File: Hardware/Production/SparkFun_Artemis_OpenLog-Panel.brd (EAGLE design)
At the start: 137.2 x 167 mm, 1942 parts, among them J105 CORTEX_JTAG, J106 MICRO-SD, J113 CORTEX_JTAG, J114 MICRO-SD, J121 CORTEX_JTAG, J122 MICRO-SD, J14 CORTEX_JTAG, J16 CORTEX_JTAG, J17 MICRO-SD, J18 MICRO-SD, J25 CORTEX_JTAG, J26 MICRO-SD, J33 CORTEX_JTAG, J34 MICRO-SD, J41 CORTEX_JTAG, J42 MICRO-SD, J49 CORTEX_JTAG, J50 MICRO-SD, J57 CORTEX_JTAG, J58 MICRO-SD, J6 CORTEX_JTAG, J65 CORTEX_JTAG, J66 MICRO-SD, J7 MICRO-SD, J73 CORTEX_JTAG, J74 MICRO-SD, J81 CORTEX_JTAG, J82 MICRO-SD, J89 CORTEX_JTAG, J90 MICRO-SD, J97 CORTEX_JTAG, J98 MICRO-SD, Q1 20V/0.2A/8MHz/1.2Ω/1Vth, Q10 20V/0.2A/8MHz/1.2Ω/1Vth, Q100 20V/0.2A/8MHz/1.2Ω/1Vth, Q101 20V/0.2A/8MHz/1.2Ω/1Vth, Q102 20V/0.2A/8MHz/1.2Ω/1Vth, Q103 20V/0.2A/8MHz/1.2Ω/1Vth, Q104 20V/4.2A/52mΩ/1.4W, Q105 20V/4.2A/52mΩ/1.4W, Q106 20V/0.2A/8MHz/1.2Ω/1Vth, Q107 20V/0.2A/8MHz/1.2Ω/1Vth, Q108 20V/0.2A/8MHz/1.2Ω/1Vth, Q109 20V/0.2A/8MHz/1.2Ω/1Vth, Q11 20V/0.2A/8MHz/1.2Ω/1Vth, Q110 20V/0.2A/8MHz/1.2Ω/1Vth, Q111 20V/4.2A/52mΩ/1.4W, Q112 20V/4.2A/52mΩ/1.4W, Q12 20V/0.2A/8MHz/1.2Ω/1Vth, Q13 20V/4.2A/52mΩ/1.4W, Q14 20V/4.2A/52mΩ/1.4W, Q15 20V/0.2A/8MHz/1.2Ω/1Vth, Q16 20V/0.2A/8MHz/1.2Ω/1Vth, Q17 20V/0.2A/8MHz/1.2Ω/1Vth, Q18 20V/0.2A/8MHz/1.2Ω/1Vth, Q19 20V/0.2A/8MHz/1.2Ω/1Vth, Q2 20V/4.2A/52mΩ/1.4W, Q20 20V/4.2A/52mΩ/1.4W, Q21 20V/4.2A/52mΩ/1.4W, Q22 20V/0.2A/8MHz/1.2Ω/1Vth, Q23 20V/0.2A/8MHz/1.2Ω/1Vth, Q24 20V/0.2A/8MHz/1.2Ω/1Vth, Q25 20V/0.2A/8MHz/1.2Ω/1Vth, Q26 20V/0.2A/8MHz/1.2Ω/1Vth, Q27 20V/4.2A/52mΩ/1.4W, Q28 20V/4.2A/52mΩ/1.4W, Q29 20V/0.2A/8MHz/1.2Ω/1Vth, Q3 20V/0.2A/8MHz/1.2Ω/1Vth, Q30 20V/0.2A/8MHz/1.2Ω/1Vth, Q31 20V/0.2A/8MHz/1.2Ω/1Vth, Q32 20V/0.2A/8MHz/1.2Ω/1Vth, Q33 20V/0.2A/8MHz/1.2Ω/1Vth, Q34 20V/4.2A/52mΩ/1.4W, Q35 20V/4.2A/52mΩ/1.4W, Q36 20V/0.2A/8MHz/1.2Ω/1Vth, Q37 20V/0.2A/8MHz/1.2Ω/1Vth, Q38 20V/0.2A/8MHz/1.2Ω/1Vth, Q39 20V/0.2A/8MHz/1.2Ω/1Vth, Q4 20V/4.2A/52mΩ/1.4W, Q40 20V/0.2A/8MHz/1.2Ω/1Vth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

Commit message: Added production files
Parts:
- removed JP17, JP19, JP21, JP23, JP25, JP27, JP29, JP31: (no value), SparkFun-Jumpers:SMT-JUMPER_2_NC_TRACE_SILK
- removed JP18, JP20, JP22, JP24, JP26, JP28, JP30, JP32: MEAS, SparkFun-Jumpers:COMBO-JUMPER_2_NC_TRACE
- removed Q100, Q101, Q102, Q103, Q106, Q107, Q108, Q109, Q110, Q99: 20V/0.2A/8MHz/1.2Ω/1Vth, SparkFun-DiscreteSemi:SOT-416FL
- removed Q104, Q105, Q111, Q112, Q97, Q98: 20V/4.2A/52mΩ/1.4W, SparkFun-DiscreteSemi:SOT23-3
- added J129, J138: (no value), SparkFun-Connectors:JST-2-SMD
- added J130, J133, J139, J142: (no value), SparkFun-Connectors:1X02_NO_SILK
- added J131, J140: (no value), SparkFun-Connectors:1X06_NO_SILK
- added J132, J141: (no value), USBC:USB-C-16P-5
- added J134, J143: MICRO-SD, SparkFun-Connectors:MICRO-SD-SOCKET
- added J135, J144: (no value), SparkFun-Connectors:1X01_NO_SILK
- added J136: CORTEX_JTAG, SparkFun-Connectors:2X5-PTH-1.27MM
- added J137: (no value), SparkFun-Connectors:JST04_1MM_RA
- added LOGO17, LOGO21, LOGO25, LOGO29, LOGO33, LOGO37, LOGO41, LOGO45, LOGO49, LOGO53, LOGO57, LOGO61: OSHW-LOGOS, SparkFun-Aesthetics:OSHW-LOGO-S
- added LOGO18, LOGO20, LOGO22, LOGO24, LOGO26, LOGO28, LOGO30, LOGO32, LOGO34, LOGO36, LOGO38, LOGO40, LOGO42, LOGO44, LOGO46, LOGO48, LOGO50, LOGO52, LOGO54, LOGO56, LOGO58, LOGO60, LOGO62, LOGO64: SFE_LOGO_FLAME.1_INCH, SparkFun-Aesthetics:SFE_LOGO_FLAME_.1
- added LOGO19, LOGO23, LOGO27, LOGO31, LOGO35, LOGO39, LOGO43, LOGO47, LOGO51, LOGO55, LOGO59, LOGO63: SFE_LOGO_NAME.1_INCH, SparkFun-Aesthetics:SFE_LOGO_NAME_.1
- added R321, R344, R367: 1M, New_Parts:0402-TIGHT
- added R322, R345, R368: 2M, New_Parts:0402-TIGHT
- added R323, R333, R334, R335, R336, R337, R338, R339, R346, R356, R357, R358, R359, R360, R361, R362: 2.2k, SparkFun-Resistors:0402-TIGHT
- added R324, R325, R326, R327, R328, R341, R347, R348, R349, R350, R351, R364: 1k, SparkFun-Resistors:0402-TIGHT
- added R329, R330, R352, R353: 5.1k, SparkFun-Resistors:0402-TIGHT
- added R331, R354: 100k, SparkFun-Resistors:0402-TIGHT
- added R332, R355: 220KOHM-0402T-1/16W-1%, SparkFun-Resistors:0402-TIGHT
- added R340, R363: DNP, SparkFun-Resistors:0402-TIGHT
- added R342, R365: 330K, New_Parts:0402-TIGHT
- added R343, R366: 220k, SparkFun-Resistors:0402-TIGHT
- added U$577: (no value), buzzard_labels (14):3V34
- added U$578, U$579: (no value), buzzard_labels (14):113
- added U$580, U$581: (no value), buzzard_labels (14):322
- added U$582, U$583: (no value), buzzard_labels (14):GND5
- added U$584, U$585: (no value), buzzard_labels (14):RX1
- added U$586, U$587: (no value), buzzard_labels (14):TX0
- added U$588, U$589: (no value), buzzard_labels:PSWC0
- added U$590: (no value), buzzard_labels (19):VE0
- added U$591, U$592: (no value), RST_04:RST0
- added U113, U121: MCP73831, SparkFun-IC-Power:SOT23-5
- added U114, U122: ARTEMIS_MODULE, SparkFun-IC-Microcontroller:ARTEMIS_FP
- added U115, U123: CH340E, SparkFun-IC-Comms:MSOP10
- added U116, U124: ICM-20948, SparkFun-Sensors:QFN24-3X3
- added U117, U125: 1.8V/100mA, SparkFun-IC-Power:SC70
- added U118, U120, U126, U128: AP2112K, SparkFun-IC-Power:SOT23-5
- added U119, U127: 3.0V Supervisor, SparkFun-IC-Power:SOT23-3
- added VE, VE1, VE10, VE11, VE12, VE13, VE14, VE15, VE2, VE3, VE4, VE5, VE6, VE7, VE8, VE9: (no value), SparkFun-Jumpers:SMT-JUMPER_2_NO_SILK
- C1, C102, C103, C111, C113, C12, C123, C124, C132, C134, C14, C144, C145, C153, C155, C165, C166, C174, C176, C186, C187, C195, C197, C2, C207, C208, C216, C218, C228, C229, C237, C239, C24, C249, C25, C250, C258, C260, C270, C271, C279, C281, C291, C292, C300, C302, C312, C313, C32, C321, C323, C333, C334, C38, C40, C45, C60, C61, C69, C71, C81, C82, C90, C92: device SparkFun-Capacitors:0603 -> SparkFun-Capacitors:0402-TIGHT
- C104, C125, C146, C167, C188, C209, C230, C251, C26, C272, C293, C314, C335, C5, C62, C83: value 10uF -> 0.1uF; device SparkFun-Capacitors:0603 -> SparkFun-Capacitors:0402-TIGHT
- C105, C126, C147, C168, C189, C210, C231, C252, C27, C273, C294, C315, C336, C63, C84: value 1.0uF -> 2.2uF
- C6: value 1.0uF -> 4.7uF
- C7: value 4.7uF -> 2.2uF
- J10, J120, J21, J48, J93: device SparkFun-Connectors:1X02_NO_SILK -> SparkFun-Connectors:JST-2-SMD
- J100, J28: value (none) -> CORTEX_JTAG; device SparkFun-Connectors:JST-2-SMD -> SparkFun-Connectors:2X5-PTH-1.27MM
- J101, J128, J29, J56: device SparkFun-Connectors:1X02_NO_SILK -> SparkFun-Connectors:JST04_1MM_RA
- J102, J30: device SparkFun-Connectors:1X06_NO_SILK -> SparkFun-Connectors:JST-2-SMD
- J103, J31, J79: device USBC:USB-C-16P-5 -> SparkFun-Connectors:1X02_NO_SILK
- J104, J32, J77: device SparkFun-Connectors:1X02_NO_SILK -> SparkFun-Connectors:1X06_NO_SILK
- J105, J33: value CORTEX_JTAG -> (none); device SparkFun-Connectors:2X5-PTH-1.27MM -> USBC:USB-C-16P-5
- J106, J34, J58: value MICRO-SD -> (none); device SparkFun-Connectors:MICRO-SD-SOCKET -> SparkFun-Connectors:1X02_NO_SILK
- J107, J35: value (none) -> MICRO-SD; device SparkFun-Connectors:JST04_1MM_RA -> SparkFun-Connectors:MICRO-SD-SOCKET
- J108, J36: device SparkFun-Connectors:JST-2-SMD -> SparkFun-Connectors:1X01_NO_SILK
- J109, J37, J64: value (none) -> CORTEX_JTAG; device SparkFun-Connectors:1X02_NO_SILK -> SparkFun-Connectors:2X5-PTH-1.27MM
- J110, J38: device SparkFun-Connectors:1X06_NO_SILK -> SparkFun-Connectors:JST04_1MM_RA
- J111, J39: device USBC:USB-C-16P-5 -> SparkFun-Connectors:JST-2-SMD
- J113, J41: value CORTEX_JTAG -> (none); device SparkFun-Connectors:2X5-PTH-1.27MM -> SparkFun-Connectors:1X06_NO_SILK
- J114, J42: value MICRO-SD -> (none); device SparkFun-Connectors:MICRO-SD-SOCKET -> USBC:USB-C-16P-5
- J115, J43, J67: device SparkFun-Connectors:JST04_1MM_RA -> SparkFun-Connectors:1X02_NO_SILK
- J116, J44: value (none) -> MICRO-SD; device SparkFun-Connectors:JST-2-SMD -> SparkFun-Connectors:MICRO-SD-SOCKET
- J117, J45, J72: device SparkFun-Connectors:1X02_NO_SILK -> SparkFun-Connectors:1X01_NO_SILK
- J118, J46: value (none) -> CORTEX_JTAG; device SparkFun-Connectors:1X06_NO_SILK -> SparkFun-Connectors:2X5-PTH-1.27MM
- J119, J47: device USBC:USB-C-16P-5 -> SparkFun-Connectors:JST04_1MM_RA
- J12, J22, J70, J94: device SparkFun-Connectors:1X06_NO_SILK -> SparkFun-Connectors:1X02_NO_SILK
- J121, J16, J25, J49, J97: value CORTEX_JTAG -> (none); device SparkFun-Connectors:2X5-PTH-1.27MM -> SparkFun-Connectors:1X02_NO_SILK
- J122, J50: value MICRO-SD -> (none); device SparkFun-Connectors:MICRO-SD-SOCKET -> SparkFun-Connectors:1X06_NO_SILK
- J123, J51: device SparkFun-Connectors:JST04_1MM_RA -> USBC:USB-C-16P-5
- J124, J52, J76: device SparkFun-Connectors:JST-2-SMD -> SparkFun-Connectors:1X02_NO_SILK
- J125, J53, J80: value (none) -> MICRO-SD; device SparkFun-Connectors:1X02_NO_SILK -> SparkFun-Connectors:MICRO-SD-SOCKET
- J126, J54: device SparkFun-Connectors:1X06_NO_SILK -> SparkFun-Connectors:1X01_NO_SILK
- J127, J55: value (none) -> CORTEX_JTAG; device USBC:USB-C-16P-5 -> SparkFun-Connectors:2X5-PTH-1.27MM
- J13, J23, J95: device USBC:USB-C-16P-5 -> SparkFun-Connectors:1X06_NO_SILK
- J15, J24, J69, J96: device SparkFun-Connectors:1X02_NO_SILK -> USBC:USB-C-16P-5
- J18, J7, J90: value MICRO-SD -> (none); device SparkFun-Connectors:MICRO-SD-SOCKET -> SparkFun-Connectors:1X01_NO_SILK
- J19, J8, J91: value (none) -> CORTEX_JTAG; device SparkFun-Connectors:JST04_1MM_RA -> SparkFun-Connectors:2X5-PTH-1.27MM
- J20, J9, J92: device SparkFun-Connectors:JST-2-SMD -> SparkFun-Connectors:JST04_1MM_RA
- J27, J99: device SparkFun-Connectors:JST04_1MM_RA -> SparkFun-Connectors:1X01_NO_SILK
- J57: value CORTEX_JTAG -> (none); device SparkFun-Connectors:2X5-PTH-1.27MM -> SparkFun-Connectors:JST-2-SMD
- J59: device SparkFun-Connectors:JST04_1MM_RA -> SparkFun-Connectors:1X06_NO_SILK
- J6, J89: value CORTEX_JTAG -> MICRO-SD; device SparkFun-Connectors:2X5-PTH-1.27MM -> SparkFun-Connectors:MICRO-SD-SOCKET
- J60: device SparkFun-Connectors:JST-2-SMD -> USBC:USB-C-16P-5
- J62: value (none) -> MICRO-SD; device SparkFun-Connectors:1X06_NO_SILK -> SparkFun-Connectors:MICRO-SD-SOCKET
- J63: device USBC:USB-C-16P-5 -> SparkFun-Connectors:1X01_NO_SILK
- J65: value CORTEX_JTAG -> (none); device SparkFun-Connectors:2X5-PTH-1.27MM -> SparkFun-Connectors:JST04_1MM_RA
- J66: value MICRO-SD -> (none); device SparkFun-Connectors:MICRO-SD-SOCKET -> SparkFun-Connectors:JST-2-SMD
- J68: device SparkFun-Connectors:JST-2-SMD -> SparkFun-Connectors:1X06_NO_SILK
- J71: value (none) -> MICRO-SD; device USBC:USB-C-16P-5 -> SparkFun-Connectors:MICRO-SD-SOCKET
- J74: value MICRO-SD -> (none); device SparkFun-Connectors:MICRO-SD-SOCKET -> SparkFun-Connectors:JST04_1MM_RA
- J75: device SparkFun-Connectors:JST04_1MM_RA -> SparkFun-Connectors:JST-2-SMD
- J78: device SparkFun-Connectors:1X06_NO_SILK -> USBC:USB-C-16P-5
- J81: value CORTEX_JTAG -> (none); device SparkFun-Connectors:2X5-PTH-1.27MM -> SparkFun-Connectors:1X01_NO_SILK
- J82: value MICRO-SD -> CORTEX_JTAG; device SparkFun-Connectors:MICRO-SD-SOCKET -> SparkFun-Connectors:2X5-PTH-1.27MM
- JP1, JP11, JP13, JP15, JP3, JP5, JP7, JP9: value (none) -> MEAS; device SparkFun-Jumpers:SMT-JUMPER_2_NC_TRACE_SILK -> SparkFun-Jumpers:COMBO-JUMPER_2_NC_TRACE
- LOGO1, LOGO11, LOGO15, LOGO7: value OSHW-LOGOS -> SFE_LOGO_NAME.1_INCH; device SparkFun-Aesthetics:OSHW-LOGO-S -> SparkFun-Aesthetics:SFE_LOGO_NAME_.1
- LOGO10, LOGO12, LOGO14, LOGO16, LOGO4, LOGO5, LOGO6, LOGO8: value OSHW-LOGOS -> SFE_LOGO_FLAME.1_INCH; device SparkFun-Aesthetics:OSHW-LOGO-S -> SparkFun-Aesthetics:SFE_LOGO_FLAME_.1
- Q12, Q18, Q24, Q30, Q36, Q54, Q60, Q66, Q72, Q78, Q96: value 20V/0.2A/8MHz/1.2Ω/1Vth -> 20V/4.2A/52mΩ/1.4W; device SparkFun-DiscreteSemi:SOT-416FL -> SparkFun-DiscreteSemi:SOT23-3
- Q13, Q14, Q20, Q21, Q27, Q28, Q34, Q35, Q4, Q41, Q49, Q55, Q56, Q62, Q63, Q69, Q70, Q76, Q77, Q83, Q91: value 20V/4.2A/52mΩ/1.4W -> 20V/0.2A/8MHz/1.2Ω/1Vth; device SparkFun-DiscreteSemi:SOT23-3 -> SparkFun-DiscreteSemi:SOT-416FL
- R100, R260: value 10k -> 5.1k
- R101, R16, R193, R216, R55, R78: value 2.2k -> 100k
- R102, R125, R263, R286, R79: value 1k -> 220KOHM-0402T-1/16W-1%
- R103, R104, R105, R106, R126, R139, R162, R185, R199, R219, R222, R223, R224, R242, R243, R244, R245, R246, R264, R265, R266, R31, R59, R62, R63, R8, R82, R83, R84, R85, R86: value 1k -> 2.2k
- R107, R108, R127, R128, R208, R247, R267, R268, R287, R288, R39: value 5.1k -> 2.2k
- R109, R129, R149, R269, R289: value 100k -> 2.2k
- R11, R12, R167, R187, R188, R42, R88: value 5.1k -> 1k
- R110: value 220k -> DNP; device SparkFun-Resistors:0603 -> SparkFun-Resistors:0402-TIGHT
- R111, R117, R118, R121, R134, R141, R157, R211, R212, R213, R232, R233, R234, R235, R236, R255, R256, R257, R258, R272, R278, R281, R295, R301, R318, R51, R52, R71, R72, R73, R74, R75, R94, R95, R96, R97, R98: value 2.2k -> 1k
- R112, R135, R158, R181, R273, R296: value 2.2k -> 330K; device SparkFun-Resistors:0402-TIGHT -> New_Parts:0402-TIGHT
- R113, R136, R251, R274, R297, R3: value 2.2k -> 220k
- R114, R137, R252, R275, R298, R91: value 2.2k -> 1M; device SparkFun-Resistors:0402-TIGHT -> New_Parts:0402-TIGHT
- R115, R138, R161, R253, R276, R92: value 2.2k -> 2M; device SparkFun-Resistors:0402-TIGHT -> New_Parts:0402-TIGHT
- R120, R140, R180, R280: value 10k -> 1k
- R122, R123, R145, R146, R283, R284, R306, R99: value 1k -> 5.1k
- R124, R239, R262, R285: value 1k -> 100k
- R13, R189, R209, R249, R43: value 100k -> 1k
- R130, R150, R270, R290, R310, R70: value 220k -> 2.2k; device SparkFun-Resistors:0603 -> SparkFun-Resistors:0402-TIGHT
- R133, R156, R271, R294, R317, R33, R49: value 2.2k -> DNP
- R14: value 220k -> 5.1k; device SparkFun-Resistors:0603 -> SparkFun-Resistors:0402-TIGHT
- R147, R308: value 5.1k -> 100k
- R148: value 5.1k -> 220KOHM-0402T-1/16W-1%
- R15, R191, R192, R214, R215, R237, R238, R261, R53, R54, R76, R77: value 2.2k -> 5.1k
- R159, R182, R205, R36: value 1k -> 220k
- R160: value 10k -> 1M; device SparkFun-Resistors:0402-TIGHT -> New_Parts:0402-TIGHT
- R169: value 100k -> 5.1k
- R17, R171, R194, R217, R56: value 2.2k -> 220KOHM-0402T-1/16W-1%
- R170: value 220k -> 100k; device SparkFun-Resistors:0603 -> SparkFun-Resistors:0402-TIGHT
- R179, R202, R225, R64: value 1k -> DNP
- R183, R206, R37, R6: value 1k -> 1M; device SparkFun-Resistors:0402-TIGHT -> New_Parts:0402-TIGHT
- R184, R299, R38, R7: value 1k -> 2M; device SparkFun-Resistors:0402-TIGHT -> New_Parts:0402-TIGHT
- R190, R210, R50: value 220k -> 1k; device SparkFun-Resistors:0603 -> SparkFun-Resistors:0402-TIGHT
- R2: value 10k -> 330K; device SparkFun-Resistors:0402-TIGHT -> New_Parts:0402-TIGHT
- R200, R220, R300, R32, R60, R80: value 10k -> 2.2k
- R204, R319, R35, R66: value 1k -> 330K; device SparkFun-Resistors:0402-TIGHT -> New_Parts:0402-TIGHT
- R207: value 5.1k -> 2M; device SparkFun-Resistors:0402-TIGHT -> New_Parts:0402-TIGHT
- R227: value 5.1k -> 330K; device SparkFun-Resistors:0402-TIGHT -> New_Parts:0402-TIGHT
- R228, R67: value 5.1k -> 220k
- R229: value 100k -> 1M; device SparkFun-Resistors:0402-TIGHT -> New_Parts:0402-TIGHT
- R230: value 220k -> 2M; device SparkFun-Resistors:0603 -> New_Parts:0402-TIGHT
- R240: value 10k -> 220KOHM-0402T-1/16W-1%
- R248, R87: value 5.1k -> DNP
- R250: value 220k -> 330K; device SparkFun-Resistors:0603 -> New_Parts:0402-TIGHT
- R29: value 220k -> 220KOHM-0402T-1/16W-1%; device SparkFun-Resistors:0603 -> SparkFun-Resistors:0402-TIGHT
- R309: value 100k -> 220KOHM-0402T-1/16W-1%
- R320: value 10k -> 220k
- R68: value 5.1k -> 1M; device SparkFun-Resistors:0402-TIGHT -> New_Parts:0402-TIGHT
- R69: value 100k -> 2M; device SparkFun-Resistors:0402-TIGHT -> New_Parts:0402-TIGHT
- R89: value 100k -> 330K; device SparkFun-Resistors:0402-TIGHT -> New_Parts:0402-TIGHT
- R90: device SparkFun-Resistors:0603 -> SparkFun-Resistors:0402-TIGHT
- U$100, U$136, U$63, U$99: device buzzard_labels (14):GND5 -> buzzard_labels (14):322
- U$101, U$102, U$138, U$65: device buzzard_labels (14):RX1 -> buzzard_labels (14):GND5
- U$103, U$104, U$140, U$67: device buzzard_labels (14):TX0 -> buzzard_labels (14):RX1
- U$105, U$69: value SPARKX-LOGO3 -> (none); device SparkX:SPARKX-SMALL -> buzzard_labels (14):TX0
- U$106, U$142: device buzzard_labels (15):LED0 -> buzzard_labels (14):TX0
- U$109: device buzzard_labels (2):MEAS3 -> buzzard_labels (19):VE0
- U$110, U$296, U$332, U$74: device buzzard_labels (1):X0 -> RST_04:RST0
- U$111, U$147, U$333, U$369: device buzzard_labels (1):Y1 -> RST_04:RST0
- U$112, U$334: device buzzard_labels (1):Z2 -> buzzard_labels (2):MEAS3
- U$113: device buzzard_labels (1):G5 -> buzzard_labels (1):X0
- U$114: device buzzard_labels (1):A4 -> buzzard_labels (1):Y1
- U$115: device buzzard_labels (1):M3 -> buzzard_labels (1):Z2
- U$116: device buzzard_labels (1):X0 -> buzzard_labels (1):G5
- U$117: device buzzard_labels (1):Y1 -> buzzard_labels (1):A4
- U$118: device buzzard_labels (1):Z2 -> buzzard_labels (1):M3
- U$119, U$335: device qwiic#logo#jpg:QWIIC#LOGO#JPG -> buzzard_labels (1):X0
- U$12, U$73: device buzzard_labels (2):MEAS3 -> RST_04:RST0
- U$120, U$336: device buzzard_labels (12):CHG2 -> buzzard_labels (1):Y1
- U$121, U$337: device buzzard_labels (12):PWR0 -> buzzard_labels (1):Z2
- U$122: device buzzard_labels (12):RX4 -> qwiic#logo#jpg:QWIIC#LOGO#JPG
- U$123: device buzzard_labels (12):STAT5 -> buzzard_labels (12):CHG2
- U$124: device buzzard_labels (12):TX3 -> buzzard_labels (12):PWR0
- U$125: device buzzard_labels (13):ARTEMIS13 -> buzzard_labels (12):RX4
- U$126: device buzzard_labels (13):OPENLOG12 -> buzzard_labels (12):STAT5
- U$127: device buzzard_labels (13):RST9 -> buzzard_labels (12):TX3
- U$128: device buzzard_labels (13):VIN8 -> buzzard_labels (13):ARTEMIS13
- U$129, U$166: device buzzard_labels (14):3V34 -> buzzard_labels (13):OPENLOG12
- U$13, U$260: device buzzard_labels (1):X0 -> buzzard_labels (2):MEAS3
- U$130, U$93: device buzzard_labels (14):3V34 -> buzzard_labels (13):RST9
- U$131, U$168: device buzzard_labels (14):113 -> buzzard_labels (13):VIN8
- U$132, U$59, U$95, U$96: device buzzard_labels (14):113 -> buzzard_labels (14):3V34
- U$133, U$169, U$170, U$206: device buzzard_labels (14):322 -> buzzard_labels (14):3V34
- U$134, U$61, U$97, U$98: device buzzard_labels (14):322 -> buzzard_labels (14):113
- U$135, U$171, U$172, U$208: device buzzard_labels (14):GND5 -> buzzard_labels (14):113
- U$137, U$173, U$174, U$210: device buzzard_labels (14):RX1 -> buzzard_labels (14):322
- U$139, U$175, U$176, U$212: device buzzard_labels (14):TX0 -> buzzard_labels (14):GND5
- U$14, U$20, U$261: device buzzard_labels (1):Y1 -> buzzard_labels (1):X0
- U$141, U$177: value SPARKX-LOGO3 -> (none); device SparkX:SPARKX-SMALL -> buzzard_labels (14):RX1
- U$143, U$179, U$180, U$216: device buzzard_labels:PSWC0 -> buzzard_labels (14):TX0
- U$145, U$181: device buzzard_labels (2):MEAS3 -> buzzard_labels:PSWC0
- U$146, U$368: device buzzard_labels (1):X0 -> buzzard_labels (19):VE0
- U$148, U$184, U$370, U$406: device buzzard_labels (1):Z2 -> RST_04:RST0
- U$149: device buzzard_labels (1):G5 -> buzzard_labels (2):MEAS3
- U$15, U$21, U$262: device buzzard_labels (1):Z2 -> buzzard_labels (1):Y1
- U$150: device buzzard_labels (1):A4 -> buzzard_labels (1):X0
- U$151: device buzzard_labels (1):M3 -> buzzard_labels (1):Y1
- U$152: device buzzard_labels (1):X0 -> buzzard_labels (1):Z2
- U$153: device buzzard_labels (1):Y1 -> buzzard_labels (1):G5
- U$154: device buzzard_labels (1):Z2 -> buzzard_labels (1):A4
- U$155: device qwiic#logo#jpg:QWIIC#LOGO#JPG -> buzzard_labels (1):M3
- U$156, U$372: device buzzard_labels (12):CHG2 -> buzzard_labels (1):X0
- U$157, U$373: device buzzard_labels (12):PWR0 -> buzzard_labels (1):Y1
- U$158, U$374: device buzzard_labels (12):RX4 -> buzzard_labels (1):Z2
- U$159: device buzzard_labels (12):STAT5 -> qwiic#logo#jpg:QWIIC#LOGO#JPG
- U$16: device buzzard_labels (1):G5 -> buzzard_labels (1):Z2
- U$160: device buzzard_labels (12):TX3 -> buzzard_labels (12):CHG2
- U$161: device buzzard_labels (13):ARTEMIS13 -> buzzard_labels (12):PWR0
- U$162: device buzzard_labels (13):OPENLOG12 -> buzzard_labels (12):RX4
- U$163: device buzzard_labels (13):RST9 -> buzzard_labels (12):STAT5
- U$164: device buzzard_labels (13):VIN8 -> buzzard_labels (12):TX3
- U$165, U$202: device buzzard_labels (14):3V34 -> buzzard_labels (13):ARTEMIS13
- U$167, U$204: device buzzard_labels (14):113 -> buzzard_labels (13):RST9
- U$17: device buzzard_labels (1):A4 -> buzzard_labels (1):G5
- U$178, U$214: device buzzard_labels (15):LED0 -> buzzard_labels (14):RX1
- U$18: device buzzard_labels (1):M3 -> buzzard_labels (1):A4
- U$182, U$218, U$404, U$440: device buzzard_labels (1):X0 -> buzzard_labels:PSWC0
- U$183, U$405: device buzzard_labels (1):Y1 -> buzzard_labels (19):VE0
- U$185, U$221: device buzzard_labels (1):G5 -> RST_04:RST0
- U$186: device buzzard_labels (1):A4 -> buzzard_labels (2):MEAS3
- U$187: device buzzard_labels (1):M3 -> buzzard_labels (1):X0
- U$188: device buzzard_labels (1):X0 -> buzzard_labels (1):Y1
- U$189: device buzzard_labels (1):Y1 -> buzzard_labels (1):Z2
- U$19: device buzzard_labels (1):X0 -> buzzard_labels (1):M3
- U$190: device buzzard_labels (1):Z2 -> buzzard_labels (1):G5
- U$191: device qwiic#logo#jpg:QWIIC#LOGO#JPG -> buzzard_labels (1):A4
- U$192: device buzzard_labels (12):CHG2 -> buzzard_labels (1):M3
- U$193, U$409: device buzzard_labels (12):PWR0 -> buzzard_labels (1):X0
- U$194, U$410: device buzzard_labels (12):RX4 -> buzzard_labels (1):Y1
- U$195, U$411: device buzzard_labels (12):STAT5 -> buzzard_labels (1):Z2
- U$196: device buzzard_labels (12):TX3 -> qwiic#logo#jpg:QWIIC#LOGO#JPG
- U$197: device buzzard_labels (13):ARTEMIS13 -> buzzard_labels (12):CHG2
- U$198: device buzzard_labels (13):OPENLOG12 -> buzzard_labels (12):PWR0
- U$199: device buzzard_labels (13):RST9 -> buzzard_labels (12):RX4
- U$200: device buzzard_labels (13):VIN8 -> buzzard_labels (12):STAT5
- U$201, U$238: device buzzard_labels (14):3V34 -> buzzard_labels (12):TX3
- U$203, U$240: device buzzard_labels (14):113 -> buzzard_labels (13):OPENLOG12
- U$205, U$242: device buzzard_labels (14):322 -> buzzard_labels (13):VIN8
- U$207, U$243, U$244, U$280: device buzzard_labels (14):GND5 -> buzzard_labels (14):3V34
- U$209, U$245, U$246, U$282: device buzzard_labels (14):RX1 -> buzzard_labels (14):113
- U$211, U$247, U$248, U$284: device buzzard_labels (14):TX0 -> buzzard_labels (14):322
- U$213, U$249: value SPARKX-LOGO3 -> (none); device SparkX:SPARKX-SMALL -> buzzard_labels (14):GND5
- U$215, U$251, U$252, U$288: device buzzard_labels:PSWC0 -> buzzard_labels (14):RX1
- U$217, U$253: device buzzard_labels (2):MEAS3 -> buzzard_labels (14):TX0
- U$219, U$255, U$441, U$477: device buzzard_labels (1):Y1 -> buzzard_labels:PSWC0
- U$22, U$263: device qwiic#logo#jpg:QWIIC#LOGO#JPG -> buzzard_labels (1):Z2
- U$220, U$442: device buzzard_labels (1):Z2 -> buzzard_labels (19):VE0
- U$222, U$258: device buzzard_labels (1):A4 -> RST_04:RST0
- U$223: device buzzard_labels (1):M3 -> buzzard_labels (2):MEAS3
- U$227: device qwiic#logo#jpg:QWIIC#LOGO#JPG -> buzzard_labels (1):G5
- U$228: device buzzard_labels (12):CHG2 -> buzzard_labels (1):A4
- U$229: device buzzard_labels (12):PWR0 -> buzzard_labels (1):M3
- U$23: device buzzard_labels (12):CHG2 -> qwiic#logo#jpg:QWIIC#LOGO#JPG
- U$230, U$446: device buzzard_labels (12):RX4 -> buzzard_labels (1):X0
- U$231, U$447: device buzzard_labels (12):STAT5 -> buzzard_labels (1):Y1
- U$232, U$448: device buzzard_labels (12):TX3 -> buzzard_labels (1):Z2
- U$233: device buzzard_labels (13):ARTEMIS13 -> qwiic#logo#jpg:QWIIC#LOGO#JPG
- U$234: device buzzard_labels (13):OPENLOG12 -> buzzard_labels (12):CHG2
- U$235: device buzzard_labels (13):RST9 -> buzzard_labels (12):PWR0
- U$236: device buzzard_labels (13):VIN8 -> buzzard_labels (12):RX4
- U$237, U$274: device buzzard_labels (14):3V34 -> buzzard_labels (12):STAT5
- U$239, U$276: device buzzard_labels (14):113 -> buzzard_labels (13):ARTEMIS13
- U$24: device buzzard_labels (12):PWR0 -> buzzard_labels (12):CHG2
- U$241, U$278: device buzzard_labels (14):322 -> buzzard_labels (13):RST9
- U$25: device buzzard_labels (12):RX4 -> buzzard_labels (12):PWR0
- U$250, U$286: device buzzard_labels (15):LED0 -> buzzard_labels (14):GND5
- U$254, U$290, U$476, U$512: device buzzard_labels (1):X0 -> buzzard_labels (14):TX0
- U$256, U$292, U$478, U$514: device buzzard_labels (1):Z2 -> buzzard_labels:PSWC0
- U$257: device buzzard_labels (1):G5 -> buzzard_labels (19):VE0
- U$259, U$295: device buzzard_labels (1):M3 -> RST_04:RST0
- U$26: device buzzard_labels (12):STAT5 -> buzzard_labels (12):RX4
- U$264: device buzzard_labels (12):CHG2 -> buzzard_labels (1):G5
- U$265: device buzzard_labels (12):PWR0 -> buzzard_labels (1):A4
- U$266: device buzzard_labels (12):RX4 -> buzzard_labels (1):M3
- U$267, U$483: device buzzard_labels (12):STAT5 -> buzzard_labels (1):X0
- U$268, U$484: device buzzard_labels (12):TX3 -> buzzard_labels (1):Y1
- U$269, U$485: device buzzard_labels (13):ARTEMIS13 -> buzzard_labels (1):Z2
- U$270: device buzzard_labels (13):OPENLOG12 -> qwiic#logo#jpg:QWIIC#LOGO#JPG
- U$271: device buzzard_labels (13):RST9 -> buzzard_labels (12):CHG2
- U$272: device buzzard_labels (13):VIN8 -> buzzard_labels (12):PWR0
- U$273, U$310: device buzzard_labels (14):3V34 -> buzzard_labels (12):RX4
- U$275, U$312: device buzzard_labels (14):113 -> buzzard_labels (12):TX3
- U$277, U$314: device buzzard_labels (14):322 -> buzzard_labels (13):OPENLOG12
- U$279, U$316: device buzzard_labels (14):GND5 -> buzzard_labels (13):VIN8
- U$281, U$317, U$318, U$354: device buzzard_labels (14):RX1 -> buzzard_labels (14):3V34
- U$283, U$319, U$320, U$356: device buzzard_labels (14):TX0 -> buzzard_labels (14):113
- U$285, U$321: value SPARKX-LOGO3 -> (none); device SparkX:SPARKX-SMALL -> buzzard_labels (14):322
- U$287, U$323, U$324, U$360: device buzzard_labels:PSWC0 -> buzzard_labels (14):GND5
- U$289, U$325: device buzzard_labels (2):MEAS3 -> buzzard_labels (14):RX1
- U$29: device buzzard_labels (12):TX3 -> buzzard_labels (12):STAT5
- U$291, U$327, U$513, U$549: device buzzard_labels (1):Y1 -> buzzard_labels (14):TX0
- U$293, U$329: device buzzard_labels (1):G5 -> buzzard_labels:PSWC0
- U$294: device buzzard_labels (1):A4 -> buzzard_labels (19):VE0
- U$297, U$75: device buzzard_labels (1):Y1 -> buzzard_labels (2):MEAS3
- U$298, U$76, U$82: device buzzard_labels (1):Z2 -> buzzard_labels (1):X0
- U$299, U$83: device qwiic#logo#jpg:QWIIC#LOGO#JPG -> buzzard_labels (1):Y1
- U$30: device buzzard_labels (13):ARTEMIS13 -> buzzard_labels (12):TX3
- U$300, U$84: device buzzard_labels (12):CHG2 -> buzzard_labels (1):Z2
- U$301: device buzzard_labels (12):PWR0 -> buzzard_labels (1):G5
- U$302: device buzzard_labels (12):RX4 -> buzzard_labels (1):A4
- U$303: device buzzard_labels (12):STAT5 -> buzzard_labels (1):M3
- U$304, U$520: device buzzard_labels (12):TX3 -> buzzard_labels (1):X0
- U$305, U$521: device buzzard_labels (13):ARTEMIS13 -> buzzard_labels (1):Y1
- U$306, U$522: device buzzard_labels (13):OPENLOG12 -> buzzard_labels (1):Z2
- U$307: device buzzard_labels (13):RST9 -> qwiic#logo#jpg:QWIIC#LOGO#JPG
- U$308: device buzzard_labels (13):VIN8 -> buzzard_labels (12):CHG2
- U$309, U$346: device buzzard_labels (14):3V34 -> buzzard_labels (12):PWR0
- U$31: device buzzard_labels (13):OPENLOG12 -> buzzard_labels (13):ARTEMIS13
- U$311, U$348: device buzzard_labels (14):113 -> buzzard_labels (12):STAT5
- U$313, U$350: device buzzard_labels (14):322 -> buzzard_labels (13):ARTEMIS13
- U$315, U$352: device buzzard_labels (14):GND5 -> buzzard_labels (13):RST9
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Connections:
- net ARTEMIS_D33 renamed SWO
- removed net ARTEMIS_D1: J6.6, U5.~AD33/SWO
- removed net ARTEMIS_D10: U16.~AD31
- removed net ARTEMIS_D11: U16.AD16
- removed net ARTEMIS_D12: U16.AD34
- removed net ARTEMIS_D13: J25.6, U23.~AD33/SWO
- removed net ARTEMIS_D14: U23.~AD29
- removed net ARTEMIS_D15: U23.~AD35
- removed net ARTEMIS_D16: U8.AD16
- removed net ARTEMIS_D17: U23.~AD31
- removed net ARTEMIS_D18: U23.AD16
- removed net ARTEMIS_D19: U23.AD34
- removed net ARTEMIS_D2: U5.~AD29
- removed net ARTEMIS_D20: J33.6, U30.~AD33/SWO
- removed net ARTEMIS_D21: U30.~AD29
- removed net ARTEMIS_D22: U30.~AD35
- removed net ARTEMIS_D23: U30.~AD31
- removed net ARTEMIS_D24: U30.AD16
- removed net ARTEMIS_D25: U30.AD34
- removed net ARTEMIS_D26: J41.6, U37.~AD33/SWO
- removed net ARTEMIS_D27: U37.~AD29
- removed net ARTEMIS_D28: U37.~AD35
- removed net ARTEMIS_D29: U8.~AD29
- removed net ARTEMIS_D3: U5.~AD35
- removed net ARTEMIS_D30: U37.~AD31
- removed net ARTEMIS_D31: U8.~AD31
- removed net ARTEMIS_D32: U37.AD16
- removed net ARTEMIS_D34: U8.AD34
- removed net ARTEMIS_D35: U8.~AD35
- removed net ARTEMIS_D36: U37.AD34
- removed net ARTEMIS_D37: J49.6, U44.~AD33/SWO
- removed net ARTEMIS_D38: U44.~AD29
- removed net ARTEMIS_D39: U44.~AD35
- removed net ARTEMIS_D4: U5.~AD31
- removed net ARTEMIS_D40: U44.~AD31
- removed net ARTEMIS_D41: U44.AD16
- removed net ARTEMIS_D42: U44.AD34
- removed net ARTEMIS_D43: J57.6, U51.~AD33/SWO
- removed net ARTEMIS_D44: U51.~AD29
- removed net ARTEMIS_D45: U51.~AD35
- removed net ARTEMIS_D46: U51.~AD31
- removed net ARTEMIS_D47: U51.AD16
- removed net ARTEMIS_D48: U51.AD34
- removed net ARTEMIS_D49: J65.6, U58.~AD33/SWO
- removed net ARTEMIS_D5: U5.AD16
- removed net ARTEMIS_D50: U58.~AD29
- removed net ARTEMIS_D51: U58.~AD35
- removed net ARTEMIS_D52: U58.~AD31
- removed net ARTEMIS_D53: U58.AD16
- removed net ARTEMIS_D54: U58.AD34
- removed net ARTEMIS_D55: J73.6, U65.~AD33/SWO
- removed net ARTEMIS_D56: U65.~AD29
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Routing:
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- added copper zone on layer 15, net 3.3V
- added copper zone on layer 15, net 3.3V1
- added copper zone on layer 15, net 3.3V10
- added copper zone on layer 15, net 3.3V11
- added copper zone on layer 15, net 3.3V12
- added copper zone on layer 15, net 3.3V13
- added copper zone on layer 15, net 3.3V14
- added copper zone on layer 15, net 3.3V15
- added copper zone on layer 15, net 3.3V2
- added copper zone on layer 15, net 3.3V3
- added copper zone on layer 15, net 3.3V4
- added copper zone on layer 15, net 3.3V5
- added copper zone on layer 15, net 3.3V6
- added copper zone on layer 15, net 3.3V7
- added copper zone on layer 15, net 3.3V8
- added copper zone on layer 15, net 3.3V9
- added copper zone on layer 15, net 5V
- added copper zone on layer 15, net 5V1
- added copper zone on layer 15, net 5V10
- added copper zone on layer 15, net 5V11
- added copper zone on layer 15, net 5V12
- added copper zone on layer 15, net 5V13
- added copper zone on layer 15, net 5V14
- added copper zone on layer 15, net 5V15
- added copper zone on layer 15, net 5V2
- added copper zone on layer 15, net 5V3
- added copper zone on layer 15, net 5V4
- added copper zone on layer 15, net 5V5
- added copper zone on layer 15, net 5V6
- added copper zone on layer 15, net 5V7
- added copper zone on layer 15, net 5V8
- added copper zone on layer 15, net 5V9
- added copper zone on layer 2, net GND
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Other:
- board size 137.2 x 167 mm -> 137.2 x 168.9 mm
- board text added: "v10"
- board text removed: "x04"

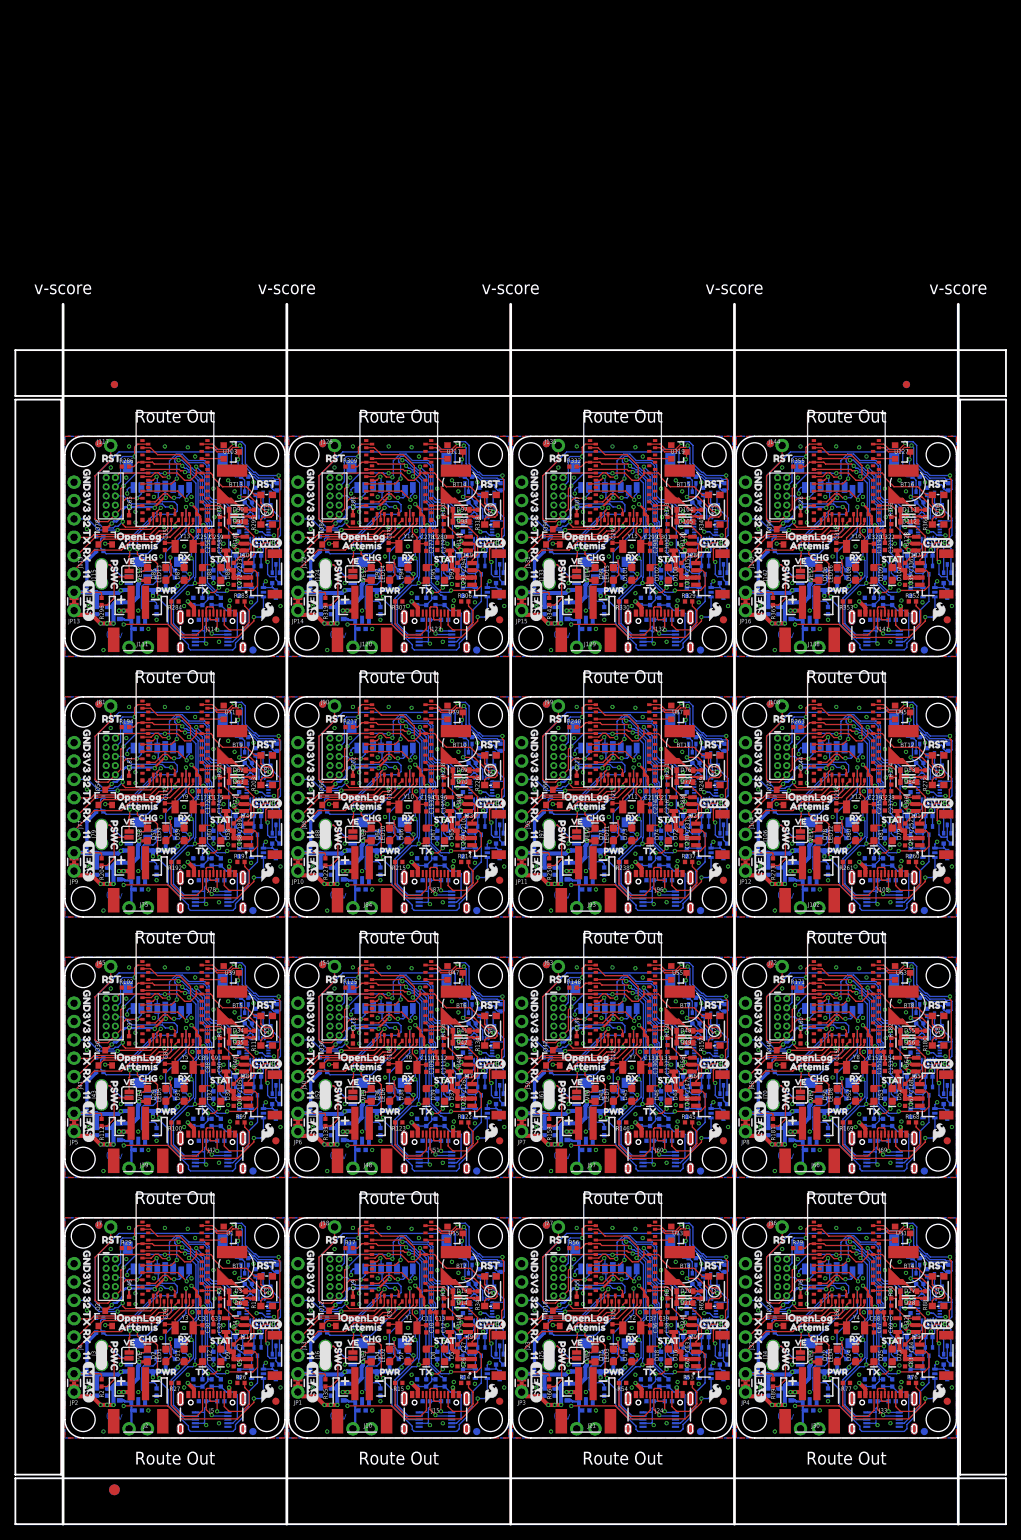
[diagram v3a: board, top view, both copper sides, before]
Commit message: Minor SCH tweaks. Replaced the USB-C connector.
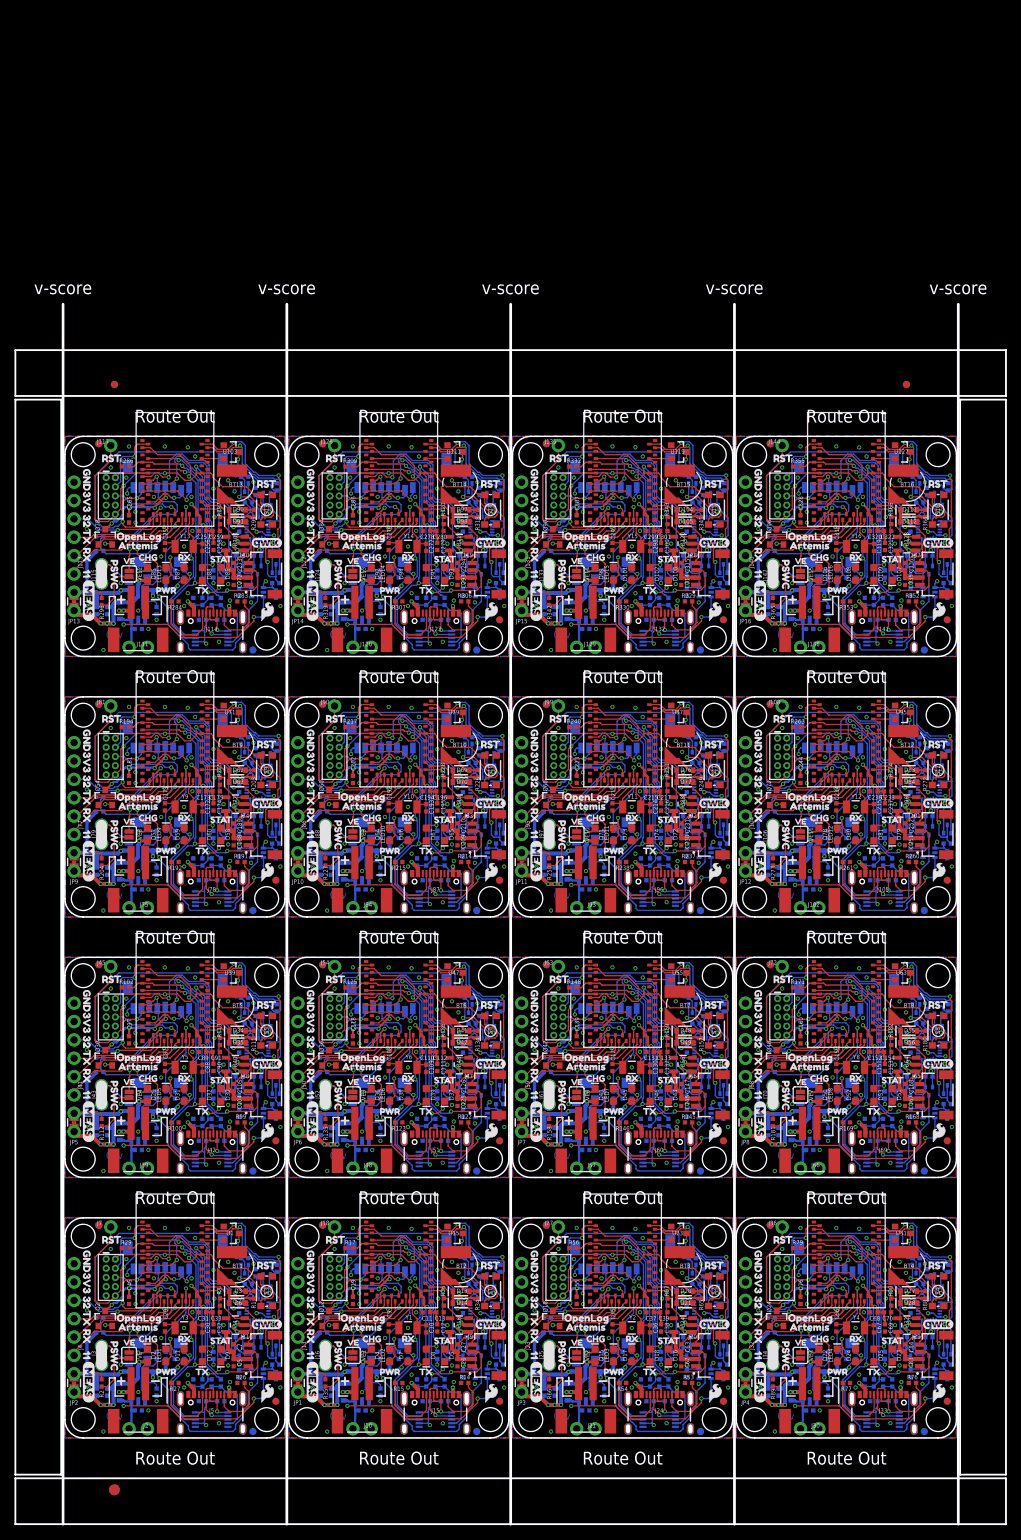
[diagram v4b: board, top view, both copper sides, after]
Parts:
- J105, J114, J123, J132, J141, J15, J24, J33, J42, J5, J51, J60, J69, J78, J87, J96: device USBC:USB-C-16P-5 -> SparkFun-Connectors:USB-C-16P_4LAYER-PADS
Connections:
- net MICROSD_!CS!/SDIO1 renamed MICROSD_!CS!1
- net MICROSD_!CS!/SDIO10 renamed MICROSD_!CS!9
- net MICROSD_!CS!/SDIO11 renamed MICROSD_!CS!10
- net MICROSD_!CS!/SDIO12 renamed MICROSD_!CS!11
- net MICROSD_!CS!/SDIO13 renamed MICROSD_!CS!12
- net MICROSD_!CS!/SDIO14 renamed MICROSD_!CS!13
- net MICROSD_!CS!/SDIO15 renamed MICROSD_!CS!14
- net MICROSD_!CS!/SDIO16 renamed MICROSD_!CS!15
- net MICROSD_!CS!/SDIO2 renamed MICROSD_!CS!2
- net MICROSD_!CS!/SDIO3 renamed MICROSD_!CS!
- net MICROSD_!CS!/SDIO4 renamed MICROSD_!CS!3
- net MICROSD_!CS!/SDIO5 renamed MICROSD_!CS!4
- net MICROSD_!CS!/SDIO6 renamed MICROSD_!CS!5
- net MICROSD_!CS!/SDIO7 renamed MICROSD_!CS!6
- net MICROSD_!CS!/SDIO8 renamed MICROSD_!CS!7
- net MICROSD_!CS!/SDIO9 renamed MICROSD_!CS!8
- net MISO/SDIO0 renamed MISO
- net MISO/SDIO1 renamed MISO1
- net MISO/SDIO10 renamed MISO10
- net MISO/SDIO11 renamed MISO11
- net MISO/SDIO12 renamed MISO12
- net MISO/SDIO13 renamed MISO13
- net MISO/SDIO14 renamed MISO14
- net MISO/SDIO15 renamed MISO15
- net MISO/SDIO2 renamed MISO2
- net MISO/SDIO3 renamed MISO3
- net MISO/SDIO4 renamed MISO4
- net MISO/SDIO5 renamed MISO5
- net MISO/SDIO6 renamed MISO6
- net MISO/SDIO7 renamed MISO7
- net MISO/SDIO8 renamed MISO8
- net MISO/SDIO9 renamed MISO9
- net MOSI/SDIO-CMD renamed MOSI
- net MOSI/SDIO-CMD1 renamed MOSI1
- net MOSI/SDIO-CMD10 renamed MOSI10
- net MOSI/SDIO-CMD11 renamed MOSI11
- net MOSI/SDIO-CMD12 renamed MOSI12
- net MOSI/SDIO-CMD13 renamed MOSI13
- net MOSI/SDIO-CMD14 renamed MOSI14
- net MOSI/SDIO-CMD15 renamed MOSI15
- net MOSI/SDIO-CMD2 renamed MOSI2
- net MOSI/SDIO-CMD3 renamed MOSI3
- net MOSI/SDIO-CMD4 renamed MOSI4
- net MOSI/SDIO-CMD5 renamed MOSI5
- net MOSI/SDIO-CMD6 renamed MOSI6
- net MOSI/SDIO-CMD7 renamed MOSI7
- net MOSI/SDIO-CMD8 renamed MOSI8
- net MOSI/SDIO-CMD9 renamed MOSI9
- net SCK/SDIO-CLK renamed SCK
- net SCK/SDIO-CLK1 renamed SCK1
- net SCK/SDIO-CLK10 renamed SCK10
- net SCK/SDIO-CLK11 renamed SCK11
- net SCK/SDIO-CLK12 renamed SCK12
- net SCK/SDIO-CLK13 renamed SCK13
- net SCK/SDIO-CLK14 renamed SCK14
- net SCK/SDIO-CLK15 renamed SCK15
- net SCK/SDIO-CLK2 renamed SCK2
- net SCK/SDIO-CLK3 renamed SCK3
- net SCK/SDIO-CLK4 renamed SCK4
- net SCK/SDIO-CLK5 renamed SCK5
- net SCK/SDIO-CLK6 renamed SCK6
- net SCK/SDIO-CLK7 renamed SCK7
- net SCK/SDIO-CLK8 renamed SCK8
- net SCK/SDIO-CLK9 renamed SCK9
- net SDIO1 renamed DAT1
- net SDIO10 renamed DAT10
- net SDIO11 renamed DAT11
- net SDIO12 renamed DAT12
- net SDIO13 renamed DAT13
- net SDIO14 renamed DAT14
- net SDIO15 renamed DAT15
- net SDIO16 renamed DAT16
- net SDIO17 renamed DAT17
- net SDIO18 renamed DAT18
- net SDIO19 renamed DAT19
- net SDIO2 renamed DAT2
- net SDIO20 renamed DAT20
- net SDIO21 renamed DAT21
- net SDIO22 renamed DAT22
- net SDIO23 renamed DAT23
- net SDIO24 renamed DAT24
- net SDIO25 renamed DAT25
- net SDIO26 renamed DAT26
- net SDIO27 renamed DAT27
- net SDIO28 renamed DAT28
- net SDIO29 renamed DAT29
- net SDIO3 renamed DAT3
- net SDIO30 renamed DAT30
- net SDIO31 renamed DAT31
- net SDIO32 renamed DAT32
- net SDIO4 renamed DAT4
- net SDIO5 renamed DAT5
- net SDIO6 renamed DAT6
- net SDIO7 renamed DAT7
- net SDIO8 renamed DAT8
- net SDIO9 renamed DAT9
- net GND: now also J5.SHLD1, J5.SHLD2, J5.SHLD3, J5.SHLD4
- net GND1: now also J15.SHLD1, J15.SHLD2, J15.SHLD3, J15.SHLD4
- net GND10: now also J96.SHLD1, J96.SHLD2, J96.SHLD3, J96.SHLD4
- net GND11: now also J105.SHLD1, J105.SHLD2, J105.SHLD3, J105.SHLD4
- net GND12: now also J114.SHLD1, J114.SHLD2, J114.SHLD3, J114.SHLD4
- net GND13: now also J123.SHLD1, J123.SHLD2, J123.SHLD3, J123.SHLD4
- net GND14: now also J132.SHLD1, J132.SHLD2, J132.SHLD3, J132.SHLD4
- net GND15: now also J141.SHLD1, J141.SHLD2, J141.SHLD3, J141.SHLD4
- net GND2: now also J24.SHLD1, J24.SHLD2, J24.SHLD3, J24.SHLD4
- net GND3: now also J33.SHLD1, J33.SHLD2, J33.SHLD3, J33.SHLD4
- net GND4: now also J42.SHLD1, J42.SHLD2, J42.SHLD3, J42.SHLD4
- net GND5: now also J51.SHLD1, J51.SHLD2, J51.SHLD3, J51.SHLD4
- net GND6: now also J60.SHLD1, J60.SHLD2, J60.SHLD3, J60.SHLD4
- net GND7: now also J69.SHLD1, J69.SHLD2, J69.SHLD3, J69.SHLD4
- net GND8: now also J78.SHLD1, J78.SHLD2, J78.SHLD3, J78.SHLD4
- net GND9: now also J87.SHLD1, J87.SHLD2, J87.SHLD3, J87.SHLD4
